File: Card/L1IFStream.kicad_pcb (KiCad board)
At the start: 4 copper layers, 88.9 x 50.8 mm, 107 parts, among them J1 Conn_Coaxial, J2 USB_A, J3 RF_Shield_One_Piece, J4 Conn_Coaxial, U1 MAX2769ETI+T, U10 74LVC374, U11 74HC2G04, U2 TPS717285DCKR, U3 TPS717285DCKR, U4 NCP164CSN330T1G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

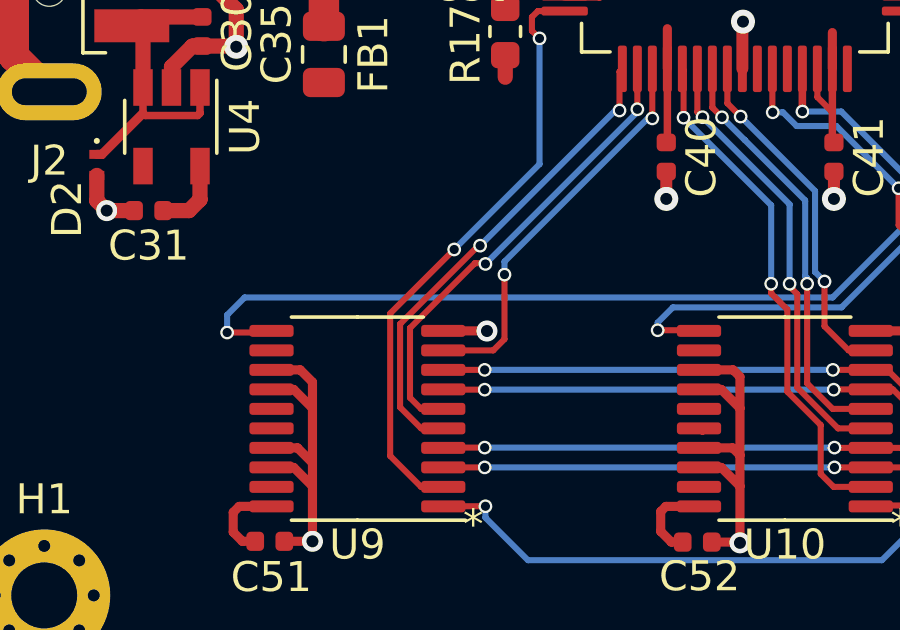
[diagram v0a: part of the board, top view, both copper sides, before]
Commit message: Flip Clocks to Reorder Nibbles
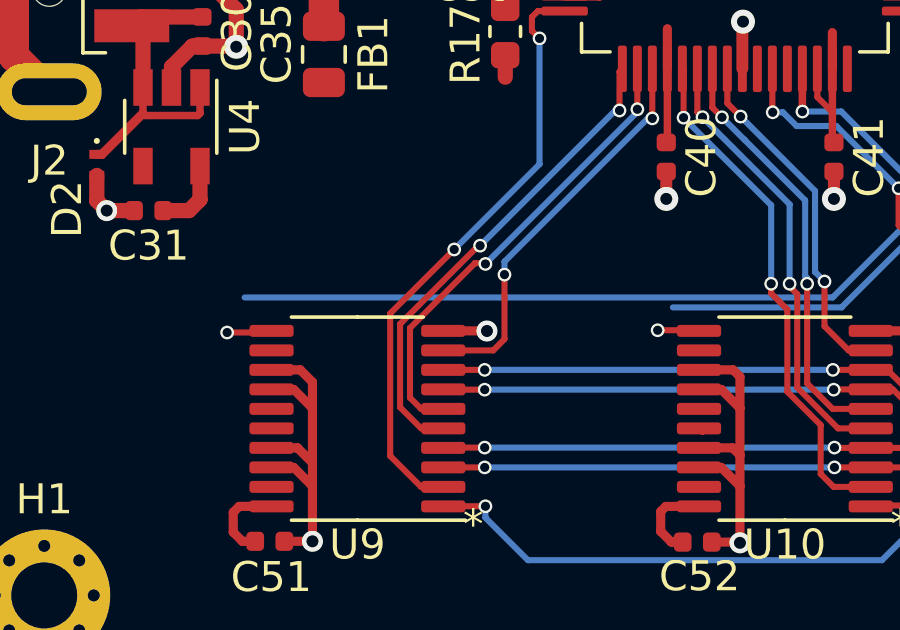
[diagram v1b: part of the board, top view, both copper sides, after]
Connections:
- U10 pad 11: /~{CLKOUT2} -> /CLKOUT2
- U9 pad 11: /CLKOUT2 -> /~{CLKOUT2}
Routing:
- net /CLKOUT2: track 44.6 -> 43.1 mm
- net /~{CLKOUT2}: track 25.9 -> 25.1 mm
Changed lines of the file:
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@@
     (title "L1IFStream")
     (date "2023-06-12")
-    (rev "v01")
+    (rev "B")
     (comment 1 "creativecommons.org/licenses/by/4.0/")
     (comment 2 "License: CC BY 4.0")
@@
       (net 4 "GND") (pinfunction "GND") (pintype "power_in"))
     (pad "11" smd roundrect (at 2.8625 2.925 180) (size 1.475 0.4) (layers "F.Cu" "F.Paste" "F.Mask") (roundrect_rratio 0.25)
-      (net 78 "/~{CLKOUT2}") (pinfunction "CLK") (pintype "input"))
+      (net 79 "/CLKOUT2") (pinfunction "CLK") (pintype "input"))
     (pad "12" smd roundrect (at 2.8625 2.275 180) (size 1.475 0.4) (layers "F.Cu" "F.Paste" "F.Mask") (roundrect_rratio 0.25)
       (net 86 "unconnected-(U10-Q4-Pad12)") (pinfunction "Q4") (pintype "tri_state+no_connect"))
@@
       (net 4 "GND") (pinfunction "GND") (pintype "power_in"))
     (pad "11" smd roundrect (at 2.8625 2.925 180) (size 1.475 0.4) (layers "F.Cu" "F.Paste" "F.Mask") (roundrect_rratio 0.25)
-      (net 79 "/CLKOUT2") (pinfunction "CLK") (pintype "input"))
+      (net 78 "/~{CLKOUT2}") (pinfunction "CLK") (pintype "input"))
     (pad "12" smd roundrect (at 2.8625 2.275 180) (size 1.475 0.4) (layers "F.Cu" "F.Paste" "F.Mask") (roundrect_rratio 0.25)
       (net 82 "unconnected-(U9-Q4-Pad12)") (pinfunction "Q4") (pintype "tri_state+no_connect"))
@@
   (segment (start 129.0472 104.1502) (end 129.5908 103.6066) (width 0.2032) (layer "F.Cu") (net 77))
   (segment (start 130.073 101.991) (end 130.073 102.641) (width 0.2032) (layer "F.Cu") (net 78))
-  (segment (start 114.5147 111.8108) (end 114.5363 111.8324) (width 0.2032) (layer "F.Cu") (net 78))
+  (segment (start 100.286 111.8322) (end 100.2865 111.8322) (width 0.2032) (layer "F.Cu") (net 78))
+  (segment (start 100.2317 111.887) (end 100.2865 111.8322) (width 0.2032) (layer "F.Cu") (net 78))
   (segment (start 130.073 102.641) (end 130.2004 102.7684) (width 0.2032) (layer "F.Cu") (net 78))
   (segment (start 130.2004 102.7684) (end 130.6068 102.7684) (width 0.2032) (layer "F.Cu") (net 78))
-  (segment (start 113.157 111.8108) (end 114.5147 111.8108) (width 0.2032) (layer "F.Cu") (net 78))
+  (segment (start 100.257 111.8612) (end 100.286 111.8322) (width 0.2032) (layer "F.Cu") (net 78))
+  (segment (start 98.806 111.887) (end 100.2317 111.887) (width 0.2032) (layer "F.Cu") (net 78))
   (segment (start 130.573 102.7346) (end 130.6068 102.7684) (width 0.2032) (layer "F.Cu") (net 78))
   (segment (start 130.573 101.991) (end 130.573 102.7346) (width 0.2032) (layer "F.Cu") (net 78))
   (via (at 130.6068 102.7684) (size 0.4572) (drill 0.3048) (layers "F.Cu" "B.Cu") (net 78))
-  (via (at 113.157 111.8108) (size 0.4572) (drill 0.3048) (layers "F.Cu" "B.Cu") (net 78))
+  (via (at 98.806 111.887) (size 0.4572) (drill 0.3048) (layers "F.Cu" "B.Cu") (net 78))
   (segment (start 119.287542 111.0488) (end 113.665 111.0488) (width 0.2032) (layer "B.Cu") (net 78))
   (segment (start 124.7648 103.648258) (end 124.7648 103.7082) (width 0.2032) (layer "B.Cu") (net 78))
-  (segment (start 113.665 111.0488) (end 113.157 111.5568) (width 0.2032) (layer "B.Cu") (net 78))
   (segment (start 130.6068 102.7684) (end 130.2258 103.1494) (width 0.2032) (layer "B.Cu") (net 78))
   (segment (start 122.7582 105.7148) (end 122.7582 107.578142) (width 0.2032) (layer "B.Cu") (net 78))
   (segment (start 122.7582 107.578142) (end 119.287542 111.0488) (width 0.2032) (layer "B.Cu") (net 78))
   (segment (start 130.2258 103.1494) (end 125.263658 103.1494) (width 0.2032) (layer "B.Cu") (net 78))
-  (segment (start 113.157 111.5568) (end 113.157 111.8108) (width 0.2032) (layer "B.Cu") (net 78))
   (segment (start 124.7648 103.7082) (end 122.7582 105.7148) (width 0.2032) (layer "B.Cu") (net 78))
   (segment (start 125.263658 103.1494) (end 124.7648 103.648258) (width 0.2032) (layer "B.Cu") (net 78))
@@
   (segment (start 124.0282 103.7082) (end 124.18639 103.86639) (width 0.2032) (layer "F.Cu") (net 79))
   (segment (start 131.073 101.311) (end 131.925 101.311) (width 0.2032) (layer "F.Cu") (net 79))
-  (segment (start 100.286 111.8322) (end 100.2865 111.8322) (width 0.2032) (layer "F.Cu") (net 79))
-  (segment (start 100.2317 111.887) (end 100.2865 111.8322) (width 0.2032) (layer "F.Cu") (net 79))
-  (segment (start 100.257 111.8612) (end 100.286 111.8322) (width 0.2032) (layer "F.Cu") (net 79))
-  (segment (start 98.806 111.887) (end 100.2317 111.887) (width 0.2032) (layer "F.Cu") (net 79))
+  (segment (start 114.5147 111.8108) (end 114.5363 111.8324) (width 0.2032) (layer "F.Cu") (net 79))
+  (segment (start 113.157 111.8108) (end 114.5147 111.8108) (width 0.2032) (layer "F.Cu") (net 79))
   (segment (start 124.191 104.9378) (end 124.18639 104.93319) (width 0.2032) (layer "F.Cu") (net 79))
   (via (at 124.0282 103.7082) (size 0.4572) (drill 0.3048) (layers "F.Cu" "B.Cu") (net 79))
   (via (at 131.925 101.311) (size 0.4572) (drill 0.3048) (layers "F.Cu" "B.Cu") (net 79))
-  (via (at 98.806 111.887) (size 0.4572) (drill 0.3048) (layers "F.Cu" "B.Cu") (net 79))
+  (via (at 113.157 111.8108) (size 0.4572) (drill 0.3048) (layers "F.Cu" "B.Cu") (net 79))
   (segment (start 131.925 101.311) (end 131.925 100.8354) (width 0.2032) (layer "B.Cu") (net 79))
   (segment (start 122.352201 107.356457) (end 122.352201 105.384199) (width 0.2032) (layer "B.Cu") (net 79))
   (segment (start 127.1524 100.584) (end 124.0282 103.7082) (width 0.2032) (layer "B.Cu") (net 79))
-  (segment (start 98.806 111.3028) (end 99.39021 110.71859) (width 0.2032) (layer "B.Cu") (net 79))
   (segment (start 131.6736 100.584) (end 127.1524 100.584) (width 0.2032) (layer "B.Cu") (net 79))
   (segment (start 131.925 100.8354) (end 131.6736 100.584) (width 0.2032) (layer "B.Cu") (net 79))
-  (segment (start 98.806 111.887) (end 98.806 111.3028) (width 0.2032) (layer "B.Cu") (net 79))
   (segment (start 122.352201 105.384199) (end 124.0282 103.7082) (width 0.2032) (layer "B.Cu") (net 79))
   (segment (start 99.39021 110.71859) (end 118.990068 110.71859) (width 0.2032) (layer "B.Cu") (net 79))

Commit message: Prepare to make new card
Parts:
- moved C29 3.87 mm to (152.7, 106.9), turned to -90 degrees
- moved X1 0.22 mm to (156.4, 106.6)
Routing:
- net /~{CLKOUT2}: track 25.1 -> 40.5 mm
- net /CLKOUT2: track 43.1 -> 30.3 mm, vias 3 -> 4
- net /2V85D: track 58.1 -> 52.4 mm
- net GND: track 144.2 -> 143.0 mm, vias 97 -> 100

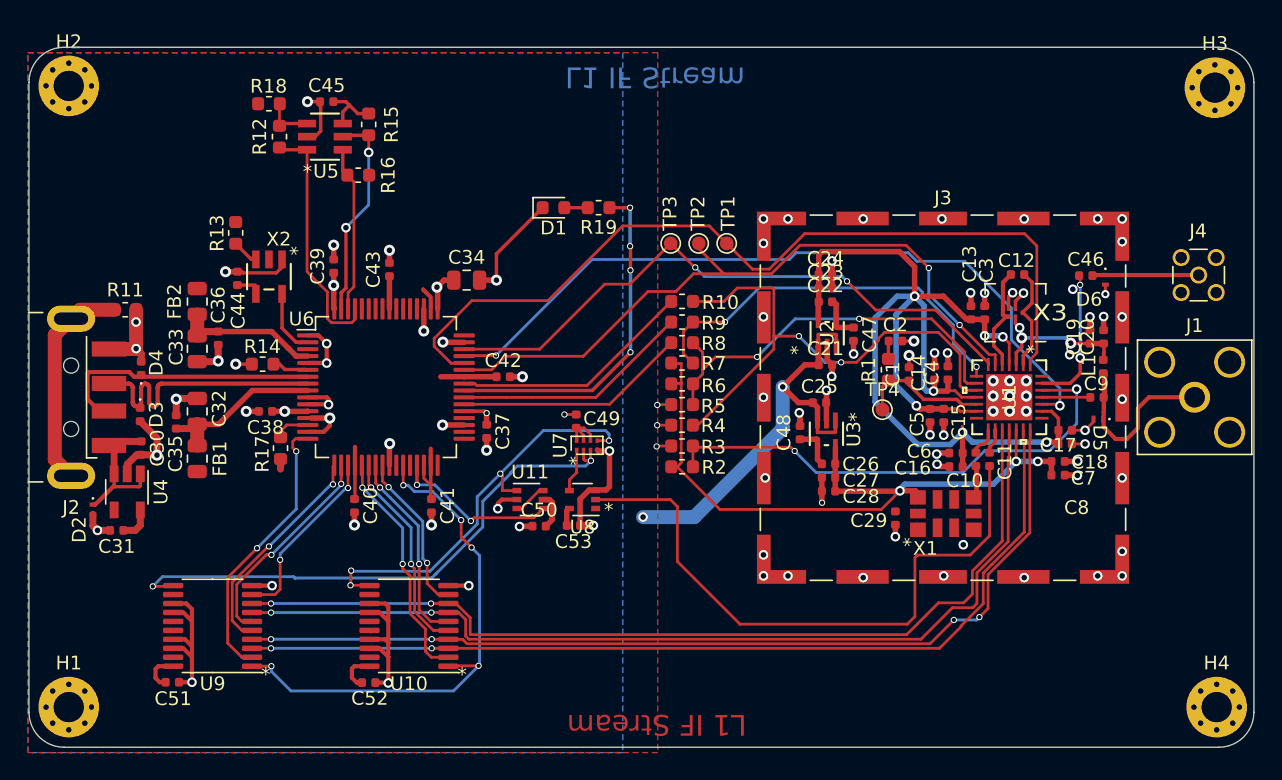
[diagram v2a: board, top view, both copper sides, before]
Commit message: Cleaned up Qorvo footprint
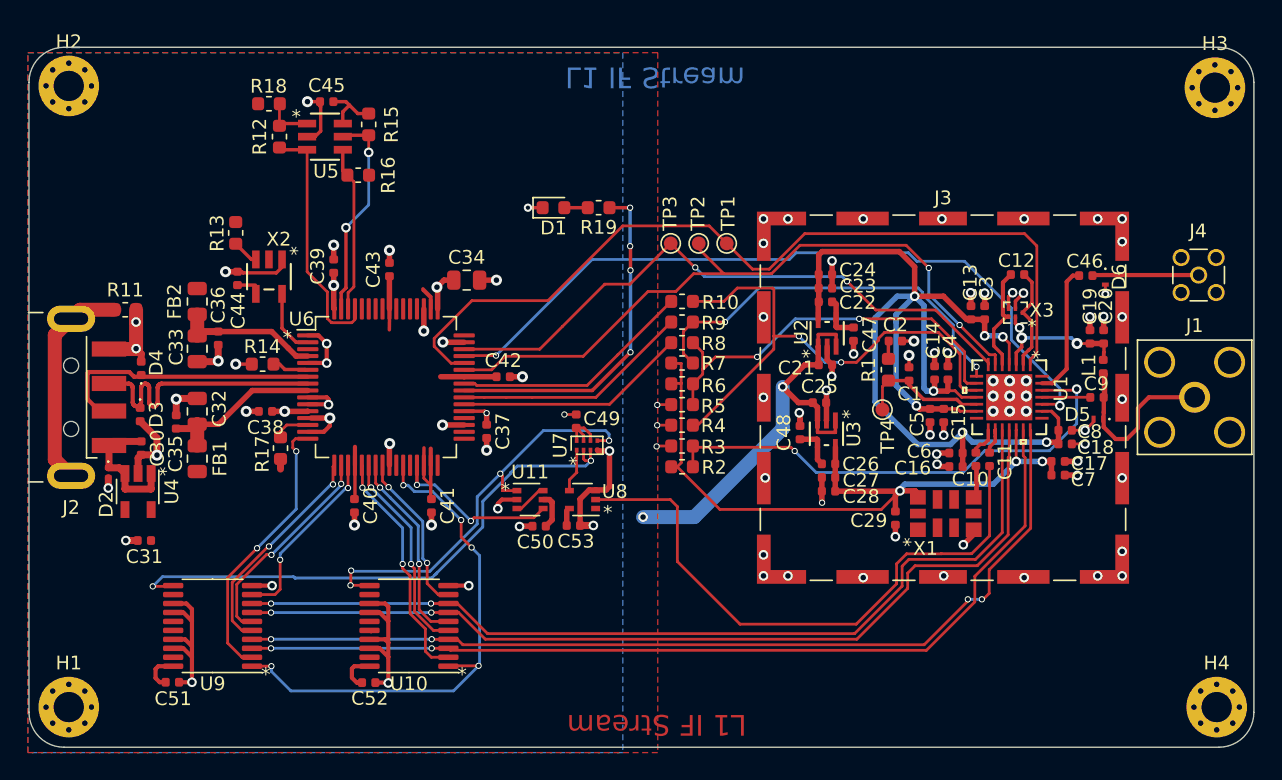
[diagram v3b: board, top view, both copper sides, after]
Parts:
- U2, U3: value TPS717285DCKR -> DCK5
- X3: footprint L1IFStream:Filter_SAW-5_1.4x1.2mm -> L1IFStream:QPQ1060_1.4x1.2
- moved D2 2.89 mm to (95.6, 103.6)
- moved C31 2.14 mm to (98.2, 108.6)
- moved U4 0.79 mm to (97.7, 105.0)
- turned C46 to 180 degrees
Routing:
- net Net-(D6-K): track 0.00 -> 7.63 mm
- net Net-(U1-LNA1): track 17.8 -> 10.4 mm, vias 2 -> 0
- net GND: track 143.0 -> 137.7 mm
- net /CLKOUT: track 44.9 -> 43.2 mm
- net /Q0: track 68.8 -> 67.1 mm
- net /2V85D: track 52.4 -> 53.8 mm
- net +3V3: track 73.6 -> 74.5 mm
- net Net-(D2-K): track 10.5 -> 9.63 mm
- net /2V85A: track 83.2 -> 82.4 mm
- net /Q1: track 67.9 -> 67.2 mm

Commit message: Verifying Footprints -- Qorvo and SiTime Checked, TVS needs minor tweaks
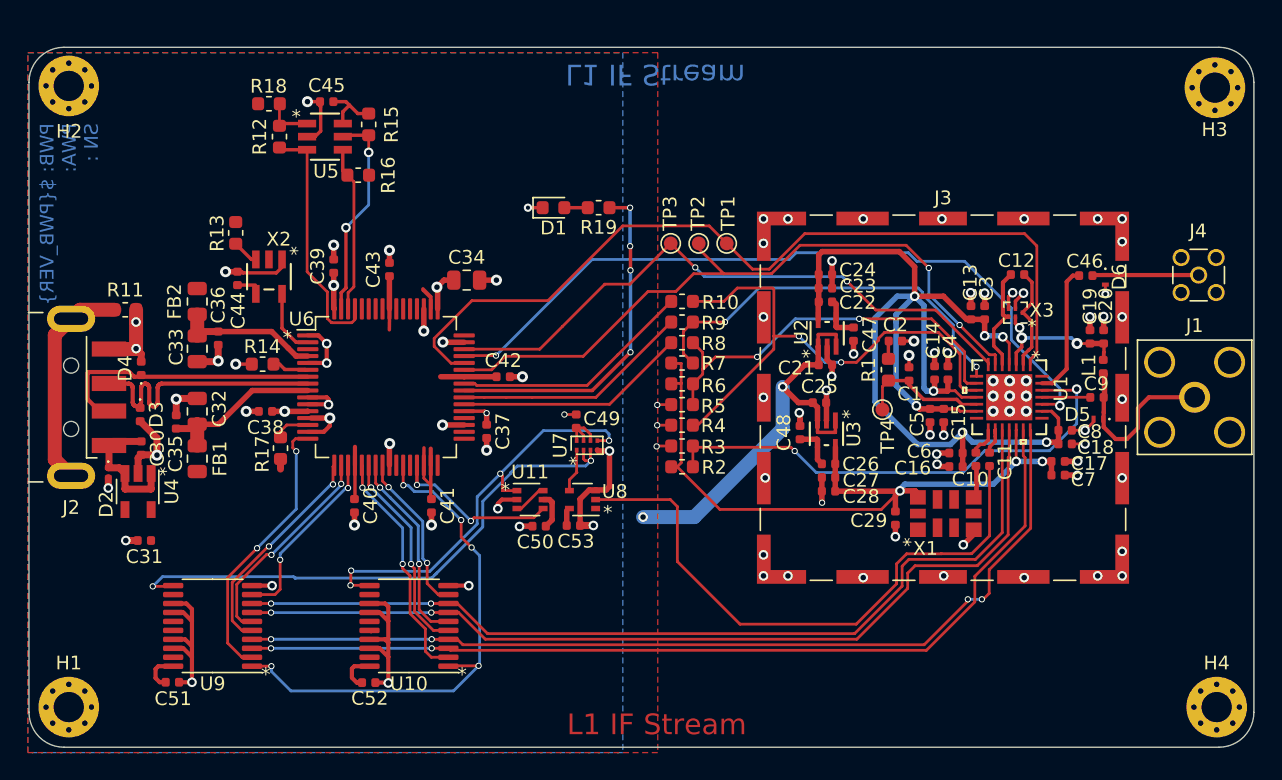
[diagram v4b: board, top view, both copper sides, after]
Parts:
- C12: value 470 pF -> NL
- C22, C26, R6: value NC -> NL
- D3, D4: footprint Diode_SMD:D_0402_1005Metric -> L1IFStream:D_0402_1005Metric
- R10, R3, R8, R9: value NC -> 0
- R2, R4, R5, R7: value 0 -> NL
- U2, U3: value DCK5 -> TPS717285DCKR
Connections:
- R19 pad 1: Net-(U6-BDBUS2) -> Net-(D1-A)
- R19 pad 2: Net-(D1-A) -> Net-(U6-BDBUS2)
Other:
- board text added: "PWB: ${PWB_VER} PWA: SN :"
- board text added: "R2 R3 R4 R5 R6 R7 R8 R9 R10 #1 0 NL 0 0 NL 0 NL NL NL Device State 2 #2 0 NL 0 NL 0 0 NL NL NL Device State 6 #3 NL 0 NL NL NL NL 0 0 0 Serial Interface"
- board text removed: "R2 R3 R4 R5 R6 R7 R8 R9 R10 #1 0 NC 0 0 NC 0 NC NC NC Device State 2 #2 0 NC 0 NC 0 0 NC NC NC Device State 6 #3 NC 0 NC NC NC NC 0 0 0 Serial Interface"

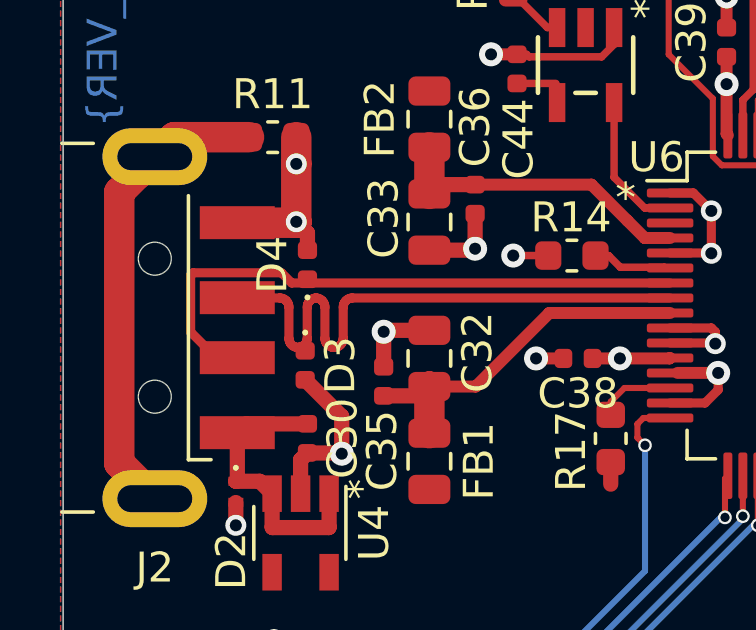
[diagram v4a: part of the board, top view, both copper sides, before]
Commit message: All new parts identified on schematic. Need minor adjustments in layout.
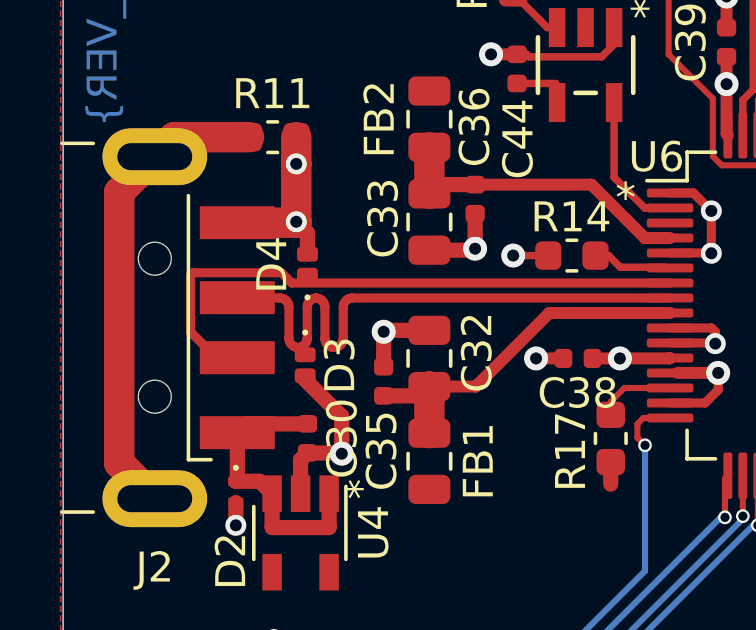
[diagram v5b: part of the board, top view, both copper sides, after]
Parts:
- D3, D4: footprint L1IFStream:D_0402_1005Metric -> L1IFStream:DPY-PX1SON_1.0mmx0.6mm
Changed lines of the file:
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@@
     )
   )
-  (footprint "L1IFStream:D_0402_1005Metric" (layer "F.Cu")
+  (footprint "L1IFStream:DPY-PX1SON_1.0mmx0.6mm" (layer "F.Cu")
     (at 97.9678 96.0628 90)
     (descr "Diode SMD 0402 (1005 Metric), square (rectangular) end terminal, IPC_7351 nominal, (Body size source: http://www.tortai-tech.com/upload/download/2011102023233369053.pdf), generated with kicad-footprint-generator")
     (tags "diode")
+    (property "Description" "TVS DIODE 3.6VWM 6.8VC 2X1SON")
+    (property "Digi-Key" "296-51108-6-ND")
+    (property "MPN" "ESD321DPYR")
     (property "Sheetfile" "L1IFStream.kicad_sch")
     (property "Sheetname" "")
@@
     (fp_line (start 0.5 0.25) (end -0.5 0.25)
       (stroke (width 0.1) (type solid)) (layer "F.Fab"))
-    (pad "1" smd roundrect (at -0.485 0 90) (size 0.59 0.64) (layers "F.Cu" "F.Paste" "F.Mask") (roundrect_rratio 0.25)
+    (pad "1" smd roundrect (at -0.35 0 90) (size 0.5 0.7) (layers "F.Cu" "F.Paste" "F.Mask") (roundrect_rratio 0.25)
       (net 62 "/D-") (pinfunction "K") (pintype "passive"))
-    (pad "2" smd roundrect (at 0.485 0 90) (size 0.59 0.64) (layers "F.Cu" "F.Paste" "F.Mask") (roundrect_rratio 0.25)
+    (pad "2" smd roundrect (at 0.35 0 90) (size 0.5 0.7) (layers "F.Cu" "F.Paste" "F.Mask") (roundrect_rratio 0.25)
       (net 4 "GND") (pinfunction "A") (pintype "passive"))
     (model "${KICAD6_3DMODEL_DIR}/Diode_SMD.3dshapes/D_0402_1005Metric.wrl"
@@
     )
   )
-  (footprint "L1IFStream:D_0402_1005Metric" (layer "F.Cu")
+  (footprint "L1IFStream:DPY-PX1SON_1.0mmx0.6mm" (layer "F.Cu")
     (at 97.8916 99.4156 -90)
     (descr "Diode SMD 0402 (1005 Metric), square (rectangular) end terminal, IPC_7351 nominal, (Body size source: http://www.tortai-tech.com/upload/download/2011102023233369053.pdf), generated with kicad-footprint-generator")
@@
     (fp_line (start 0.5 0.25) (end -0.5 0.25)
       (stroke (width 0.1) (type solid)) (layer "F.Fab"))
-    (pad "1" smd roundrect (at -0.485 0 270) (size 0.59 0.64) (layers "F.Cu" "F.Paste" "F.Mask") (roundrect_rratio 0.25)
+    (pad "1" smd roundrect (at -0.35 0 270) (size 0.5 0.7) (layers "F.Cu" "F.Paste" "F.Mask") (roundrect_rratio 0.25)
       (net 61 "/D+") (pinfunction "K") (pintype "passive"))
-    (pad "2" smd roundrect (at 0.485 0 270) (size 0.59 0.64) (layers "F.Cu" "F.Paste" "F.Mask") (roundrect_rratio 0.25)
+    (pad "2" smd roundrect (at 0.35 0 270) (size 0.5 0.7) (layers "F.Cu" "F.Paste" "F.Mask") (roundrect_rratio 0.25)
       (net 4 "GND") (pinfunction "A") (pintype "passive"))
     (model "${KICAD6_3DMODEL_DIR}/Diode_SMD.3dshapes/D_0402_1005Metric.wrl"

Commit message: Ready for prototype quote
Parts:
- added G***: LOGO, L1IFStream:Signature-Kyle, F.Cu at (174.1, 109.5)
- moved D3 0.98 mm to (98.9, 99.3)
- moved D4 0.90 mm to (98.9, 96.2)
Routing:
- net GND: track 137.7 -> 137.1 mm
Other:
- board text added: "PWB: ${PWB_VER} PWA: ] SN : ]"
- board text removed: "PWB: ${PWB_VER} PWA: SN :"
